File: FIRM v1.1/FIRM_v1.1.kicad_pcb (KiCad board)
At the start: 8 copper layers, 70 parts, among them J2 Conn_01x02_Pin, Q1 IRLML6402, U1 W25N04KVZEIR, U2 STM32H743VIHx, U3 ADXL371, U5 INA219AxDCN, U6 MIC5219-3.3YM5, U9 A-USBC-20F0-EA-GSR05, X1 32.768khz, Y1 12 MHz

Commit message: Added new flash chip
Set up quadSPI with the new 1gbit flash chip.
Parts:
- removed U1: W25N04KVZEIR, IC_W25N04KVZEIR:IC_W25N04KVZEIR

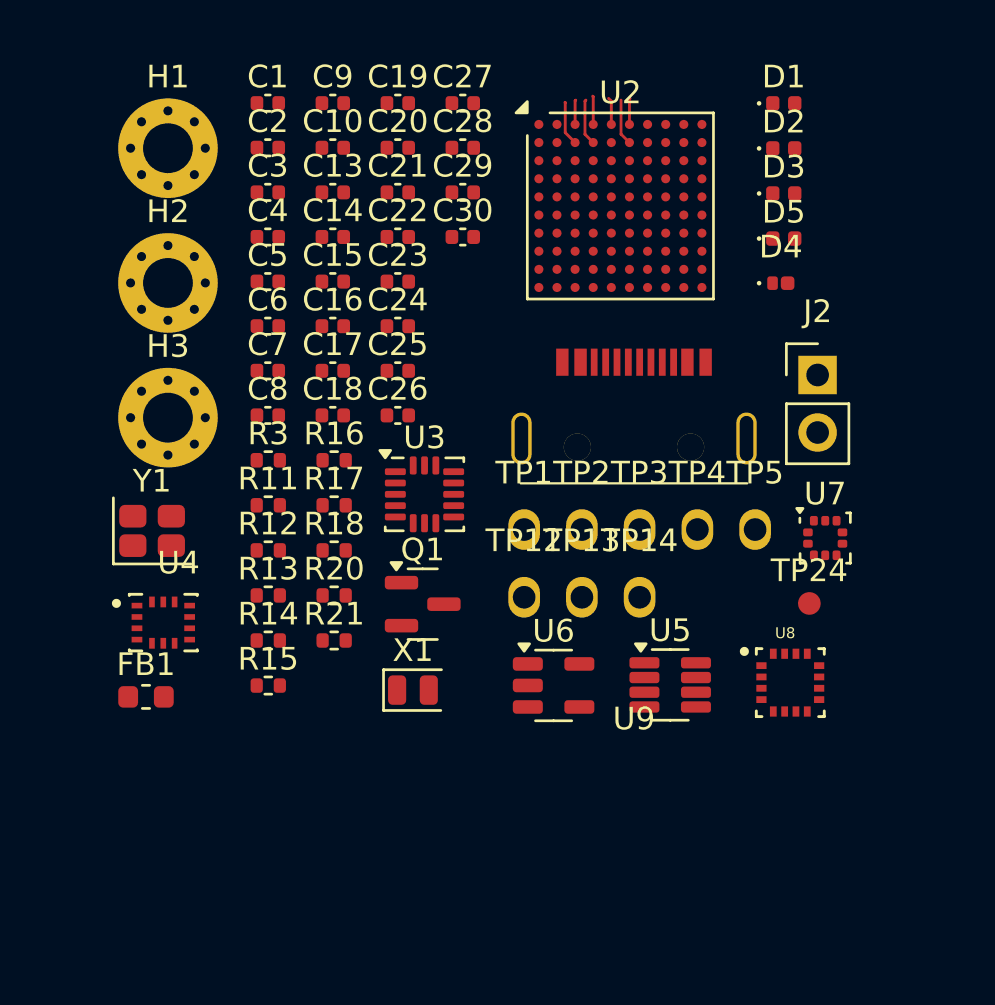
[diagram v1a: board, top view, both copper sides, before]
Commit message: added design rules
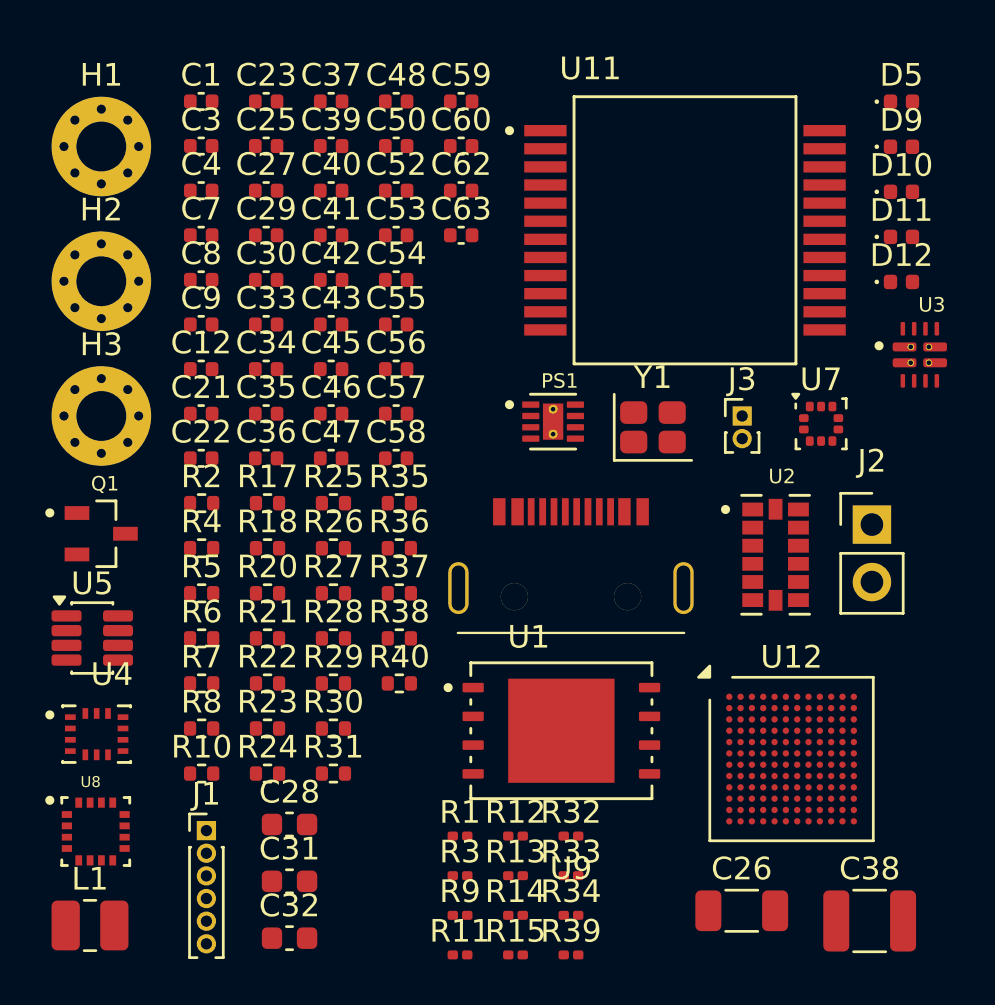
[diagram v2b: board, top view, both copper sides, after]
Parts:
- removed C10, C5: 14p, Capacitor_SMD:C_0402_1005Metric
- removed C13, C15, C17, C19, C20, C6: 100n, Capacitor_SMD:C_0402_1005Metric
- removed C14: 2u2, Capacitor_SMD:C_0402_1005Metric
- removed C16: 10n, Capacitor_SMD:C_0402_1005Metric
- removed C18: 1u, Capacitor_SMD:C_0402_1005Metric
- removed C2: 4u7, Capacitor_SMD:C_0402_1005Metric
- removed C24: 10u, Capacitor_SMD:C_0402_1005Metric
- removed D1: LED_Blue, LED_SMD:LED_0402_1005Metric
- removed D2: LED_Yellow, LED_SMD:LED_0402_1005Metric
- removed D3: LED_Red, LED_SMD:LED_0402_1005Metric
- removed D4: D_Schottky, connectors:D_schottky_NSR05F30NXT5G
- removed FB1: 120 Ohms @ 100 MHz, Inductor_SMD:L_0603_1608Metric
- removed R16: 100k, Resistor_SMD:R_0402_1005Metric
- removed TP1: PA0 Test Point, connectors:Testpoint_1.5x1.5mm_1.0mm
- removed TP12: SWDIO Through-Hole, connectors:Testpoint_1.5x1.5mm_1.0mm
- removed TP13: SWCLK Through-Hole, connectors:Testpoint_1.5x1.5mm_1.0mm
- removed TP14: 3.3V Test Point, connectors:Testpoint_1.5x1.5mm_1.0mm
- removed TP2: PA1 Test Point, connectors:Testpoint_1.5x1.5mm_1.0mm
- removed TP24: NRST Pad, connectors:smd_test_pads_1mm
- removed TP3: PA2 Test Point, connectors:Testpoint_1.5x1.5mm_1.0mm
- removed TP4: PA9 Test Point, connectors:Testpoint_1.5x1.5mm_1.0mm
- removed TP5: PA10 Test Point, connectors:Testpoint_1.5x1.5mm_1.0mm
- removed U6: MIC5219-3.3YM5, Package_TO_SOT_SMD:SOT-23-5
- removed X1: 32.768khz, connectors:Crystal_ECS-.327-6-12RR-TR
- added C12: 100n, Capacitor_SMD:C_0402_1005Metric, F.Cu at (140.8, 71.4)
- added C31: 22u, Capacitor_SMD:C_0603_1608Metric, F.Cu at (144.7, 94.0)
- added C32: 10u, Capacitor_SMD:C_0603_1608Metric, F.Cu at (144.7, 96.5)
- added C33: 1u, Capacitor_SMD:C_0402_1005Metric, F.Cu at (143.7, 69.4)
- added C34: 100n, Capacitor_SMD:C_0402_1005Metric, F.Cu at (143.7, 71.4)
- added C35: 100n, Capacitor_SMD:C_0402_1005Metric, F.Cu at (143.7, 73.4)
- added C36: 100n, Capacitor_SMD:C_0402_1005Metric, F.Cu at (143.7, 75.3)
- added C37: 1u, Capacitor_SMD:C_0402_1005Metric, F.Cu at (146.5, 59.6)
- added C38: 22u, Capacitor_SMD:C_1210_3225Metric, F.Cu at (170.3, 95.8)
- added C39: 100n, Capacitor_SMD:C_0402_1005Metric, F.Cu at (146.5, 61.6)
- added C40: 100n, Capacitor_SMD:C_0402_1005Metric, F.Cu at (146.5, 63.5)
- added C41: 100n, Capacitor_SMD:C_0402_1005Metric, F.Cu at (146.5, 65.5)
- added C42: 100n, Capacitor_SMD:C_0402_1005Metric, F.Cu at (146.5, 67.5)
- added C43: 100n, Capacitor_SMD:C_0402_1005Metric, F.Cu at (146.5, 69.4)
- added C45: 100n, Capacitor_SMD:C_0402_1005Metric, F.Cu at (146.5, 71.4)
- added C46: 14p, Capacitor_SMD:C_0402_1005Metric, F.Cu at (146.5, 73.4)
- added C47: 14p, Capacitor_SMD:C_0402_1005Metric, F.Cu at (146.5, 75.3)
- added C48: 100n, Capacitor_SMD:C_0402_1005Metric, F.Cu at (149.4, 59.6)
- added C50: 2u2, Capacitor_SMD:C_0402_1005Metric, F.Cu at (149.4, 61.6)
- added C52: 100n, Capacitor_SMD:C_0402_1005Metric, F.Cu at (149.4, 63.5)
- added C53: 2u2, Capacitor_SMD:C_0402_1005Metric, F.Cu at (149.4, 65.5)
- added C54: 100n, Capacitor_SMD:C_0402_1005Metric, F.Cu at (149.4, 67.5)
- added C55: 100n, Capacitor_SMD:C_0402_1005Metric, F.Cu at (149.4, 69.4)
- added C56: 1u, Capacitor_SMD:C_0402_1005Metric, F.Cu at (149.4, 71.4)
- added C57: 1u, Capacitor_SMD:C_0402_1005Metric, F.Cu at (149.4, 73.4)
- added C58: 100n, Capacitor_SMD:C_0402_1005Metric, F.Cu at (149.4, 75.3)
- added C59: 1u, Capacitor_SMD:C_0402_1005Metric, F.Cu at (152.3, 59.6)
- added C60: 1u, Capacitor_SMD:C_0402_1005Metric, F.Cu at (152.3, 61.6)
- added C62: 10u, Capacitor_SMD:C_0402_1005Metric, F.Cu at (152.3, 63.5)
- added C63: 1u, Capacitor_SMD:C_0402_1005Metric, F.Cu at (152.3, 65.5)
- added D10: LED_Yellow, LED_SMD:LED_0402_1005Metric, F.Cu at (171.7, 63.6)
- added D11: LED_Red, LED_SMD:LED_0402_1005Metric, F.Cu at (171.7, 65.6)
- added D12: LED_Green, LED_SMD:LED_0402_1005Metric, F.Cu at (171.7, 67.6)
- added D9: LED_Blue, LED_SMD:LED_0402_1005Metric, F.Cu at (171.7, 61.6)
- added J1: Pin, Connector_PinHeader_1.00mm:PinHeader_1x06_P1.00mm_Vertical, F.Cu at (141.0, 91.8)
- added J3: FIRM2 Conn, Connector_PinHeader_1.00mm:PinHeader_1x02_P1.00mm_Vertical, F.Cu at (164.7, 73.5)
- added L1: 2u2, Inductor_SMD:L_1008_2520Metric, F.Cu at (135.9, 96.0)
- added PS1: TPS62162DSGR, HPRC_Regulators:TPS62162DSGR, F.Cu at (156.3, 73.7)
- added R1: 0, Resistor_SMD:R_0201_0603Metric, F.Cu at (152.2, 92.0)
- added R10: 1k2, Resistor_SMD:R_0402_1005Metric, F.Cu at (140.8, 89.3)
- added R2: 10k, Resistor_SMD:R_0402_1005Metric, F.Cu at (140.8, 77.3)
- added R22: 10k, Resistor_SMD:R_0402_1005Metric, F.Cu at (143.7, 85.3)
- added R23: 10k, Resistor_SMD:R_0402_1005Metric, F.Cu at (143.7, 87.3)
- added R24: 10k, Resistor_SMD:R_0402_1005Metric, F.Cu at (143.7, 89.3)
- added R25: 10k, Resistor_SMD:R_0402_1005Metric, F.Cu at (146.6, 77.3)
- added R26: 100k, Resistor_SMD:R_0402_1005Metric, F.Cu at (146.6, 79.3)
- added R27: 100k, Resistor_SMD:R_0402_1005Metric, F.Cu at (146.6, 81.3)
- added R28: 80k, Resistor_SMD:R_0402_1005Metric, F.Cu at (146.6, 83.3)
- added R29: 100k, Resistor_SMD:R_0402_1005Metric, F.Cu at (146.6, 85.3)
- added R30: 7k6, Resistor_SMD:R_0402_1005Metric, F.Cu at (146.6, 87.3)
- added R31: 57.6k, Resistor_SMD:R_0402_1005Metric, F.Cu at (146.6, 89.3)
- added R32: 0, Resistor_SMD:R_0201_0603Metric, F.Cu at (157.1, 92.0)
- added R33: 0, Resistor_SMD:R_0201_0603Metric, F.Cu at (157.1, 93.8)
- added R34: 0, Resistor_SMD:R_0201_0603Metric, F.Cu at (157.1, 95.5)
- added R35: 5.1k, Resistor_SMD:R_0402_1005Metric, F.Cu at (149.5, 77.3)
- added R36: 10k, Resistor_SMD:R_0402_1005Metric, F.Cu at (149.5, 79.3)
- added R37: 32k, Resistor_SMD:R_0402_1005Metric, F.Cu at (149.5, 81.3)
- added R38: 100k, Resistor_SMD:R_0402_1005Metric, F.Cu at (149.5, 83.3)
- added R39: 0, Resistor_SMD:R_0201_0603Metric, F.Cu at (157.1, 97.3)
- added R4: 3k3, Resistor_SMD:R_0402_1005Metric, F.Cu at (140.8, 79.3)
- added R40: 1k, Resistor_SMD:R_0402_1005Metric, F.Cu at (149.5, 85.3)
- added R5: 3k3, Resistor_SMD:R_0402_1005Metric, F.Cu at (140.8, 81.3)
- added R6: 1.2k, Resistor_SMD:R_0402_1005Metric, F.Cu at (140.8, 83.3)
- added R7: 1k2, Resistor_SMD:R_0402_1005Metric, F.Cu at (140.8, 85.3)
- added R8: 1k2, Resistor_SMD:R_0402_1005Metric, F.Cu at (140.8, 87.3)
- added R9: 0, Resistor_SMD:R_0201_0603Metric, F.Cu at (152.2, 95.5)
- added U1: W25N01KVZEIR, HPRC_Storage:W25N01KVZEIR, F.Cu at (156.7, 87.4)
- added U11: SCH16T-K01-10, HPRC_Sensors:XDCR_SCH16T-K01-10, F.Cu at (162.2, 65.3)
- added U12: STM32F446ZCH6, Package_BGA:UFBGA-144_7x7mm_Layout12x12_P0.5mm, F.Cu at (166.9, 88.6)
- C26: value 470p -> 10u; footprint Capacitor_SMD:C_0402_1005Metric -> Capacitor_SMD:C_1206_3216Metric
- C28: footprint Capacitor_SMD:C_0402_1005Metric -> Capacitor_SMD:C_0603_1608Metric
- C4: value 6p -> 4u7
- C7: value 6p -> 100n
- C9: value 2u2 -> 100n
- J2: value Conn_01x02_Pin -> Vbat Jmpr; footprint connectors:power_headers -> HPRC_Connectors:power_headers
- Q1: value IRLML6402 -> DMP3098L-7; footprint Package_TO_SOT_SMD:SOT-23 -> HPRC_Logic:DMP3098L-7
- R11, R12: value 3k3 -> 0; footprint Resistor_SMD:R_0402_1005Metric -> Resistor_SMD:R_0201_0603Metric
- R13: value 1.2k -> 0; footprint Resistor_SMD:R_0402_1005Metric -> Resistor_SMD:R_0201_0603Metric
- R14, R15: value 1k2 -> 0; footprint Resistor_SMD:R_0402_1005Metric -> Resistor_SMD:R_0201_0603Metric
- R17: value 10m -> 100m
- R3: value 100k -> 0; footprint Resistor_SMD:R_0402_1005Metric -> Resistor_SMD:R_0201_0603Metric
- U2: value STM32H743VIHx -> ADXL375; footprint Package_BGA:TFBGA-100_8x8mm_Layout10x10_P0.8mm -> HPRC_Sensors:ADXL375BCCZ-RL7
- U3: value ADXL371 -> TPS2121RUXR; footprint Sensor_Motion:Analog_LGA-16_3.25x3mm_P0.5mm_LayoutBorder3x5y -> HPRC_Regulators:IC_TPS2121RUXR
- U4: value ~ -> ICM45686; footprint sensors:IC_ICM-45686 -> HPRC_Sensors:IC_ICM-45686
- U7: value ~ -> BMP581; footprint sensors:BMPFootprintNoSolderMask -> HPRC_Sensors:BMP581
- U8: value ~ -> MMC5983MA; footprint sensors:IC_MMC5983MA -> HPRC_Sensors:IC_MMC5983MA
- U9: footprint connectors:A-USBC-20F0-EA-GSR05 -> HPRC_Connectors:A-USBC-20F0-EA-GSR05
- Y1: footprint connectors:Crystal_ECS-120-10-36B2-CWY-TR -> HPRC_Connectors:Crystal_ECS-120-10-36B2-CWY-TR
- moved U8 31.4 mm to (136.1, 91.8)
- moved C28 30.8 mm to (144.7, 91.5)
- moved C26 26.6 mm to (164.7, 95.3)
- moved U5 25.6 mm to (136.0, 83.3)
- moved U3 22.7 mm to (172.5, 70.8)
- moved Y1 22.6 mm to (160.7, 74.0)
- moved R11 21.6 mm to (152.2, 97.3)
- moved R3 20.2 mm to (152.2, 93.8)
- moved U2 16.9 mm to (166.2, 79.6)
- moved R12 16.7 mm to (154.7, 92.0)
- moved R13 16.5 mm to (154.7, 93.8)
- moved R14 16.3 mm to (154.7, 95.5)
- moved R15 16.1 mm to (154.7, 97.3)
- moved Q1 14.5 mm to (136.4, 78.7)
- moved C22 13.1 mm to (140.8, 75.3)
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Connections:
- net VBAT renamed Net-(J2-Pin_1)
- C1 pad 1: unconnected-(C1-Pad1) -> +3.3V
- C26 pad 1: Net-(U6-BP) -> /VSENS_OUT
- C28 pad 1: +3.3V -> VBUS
- C4 pad 1: Net-(C4-Pad1) -> +3.3V
- C7 pad 1: Net-(C7-Pad1) -> +3.3V
- C9 pad 1: unconnected-(C9-Pad1) -> +3.3V
- Q1 pad 1: VBUS -> Net-(Q1-Pad1)
- Q1 pad 2: /VSENS_IN -> GND
- R11 pad 1: unconnected-(R11-Pad1) -> /QUADSPI_BK1_IO3
- R11 pad 2: +3.3V -> Net-(U12-PF6)
- R12 pad 1: unconnected-(R12-Pad1) -> Net-(U12-PF7)
- R12 pad 2: +3.3V -> /QUADSPI_BK1_IO2
- R13 pad 2: /DBUG_0 -> /QUADSPI_BK1_IO1
- R14 pad 2: /DBUG_1 -> /QUADSPI_BK1_IO0
- R15 pad 2: /DBUG_2 -> /SCK3
- R3 pad 1: unconnected-(R3-Pad1) -> /MISO2
- R3 pad 2: GND -> Net-(U12-PC2)
- U3 pad 1: +3.3V -> /VSENS_IN
- U3 pad 10: unconnected-(U3-GND-Pad13) -> Net-(U3-ILIM)
- U3 pad 11: /HIG_INT -> Net-(U3-SS)
- U3 pad 2: unconnected-(U3-NIC-Pad2) -> GND
- U3 pad 3: unconnected-(U3-RES-Pad3) -> Net-(U3-CP2)
- U3 pad 4: /SCK2 -> Net-(U3-OV2)
- U3 pad 5: unconnected-(U3-RES-Pad5) -> GND
- U3 pad 6: /MOSI2 -> Net-(U3-PR1)
- U3 pad 7: /MISO2 -> VBUS
- U3 pad 8: /HIG_CS -> /VSENS_IN
- U3 pad 9: unconnected-(U3-INT2-Pad9) -> GND
- Y1 pad 1: Net-(C5-Pad1) -> /RCC_OSC_IN
- Y1 pad 3: Net-(C10-Pad1) -> /RCC_OSC_OUT
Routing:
- net unconnected-(U2-PB8-PadB4): track 2.04 -> 0.00 mm
- net unconnected-(U2-PD5-PadB6): track 2.03 -> 0.00 mm
- net unconnected-(U2-PE3-PadB3): track 1.96 -> 0.00 mm
- net unconnected-(U2-PB9-PadA4): track 1.26 -> 0.00 mm
- net unconnected-(U2-PB7-PadA5): track 1.20 -> 0.00 mm
- net unconnected-(U2-PB4-PadA6): track 1.16 -> 0.00 mm
- net unconnected-(U2-PE2-PadA3): track 1.09 -> 0.00 mm

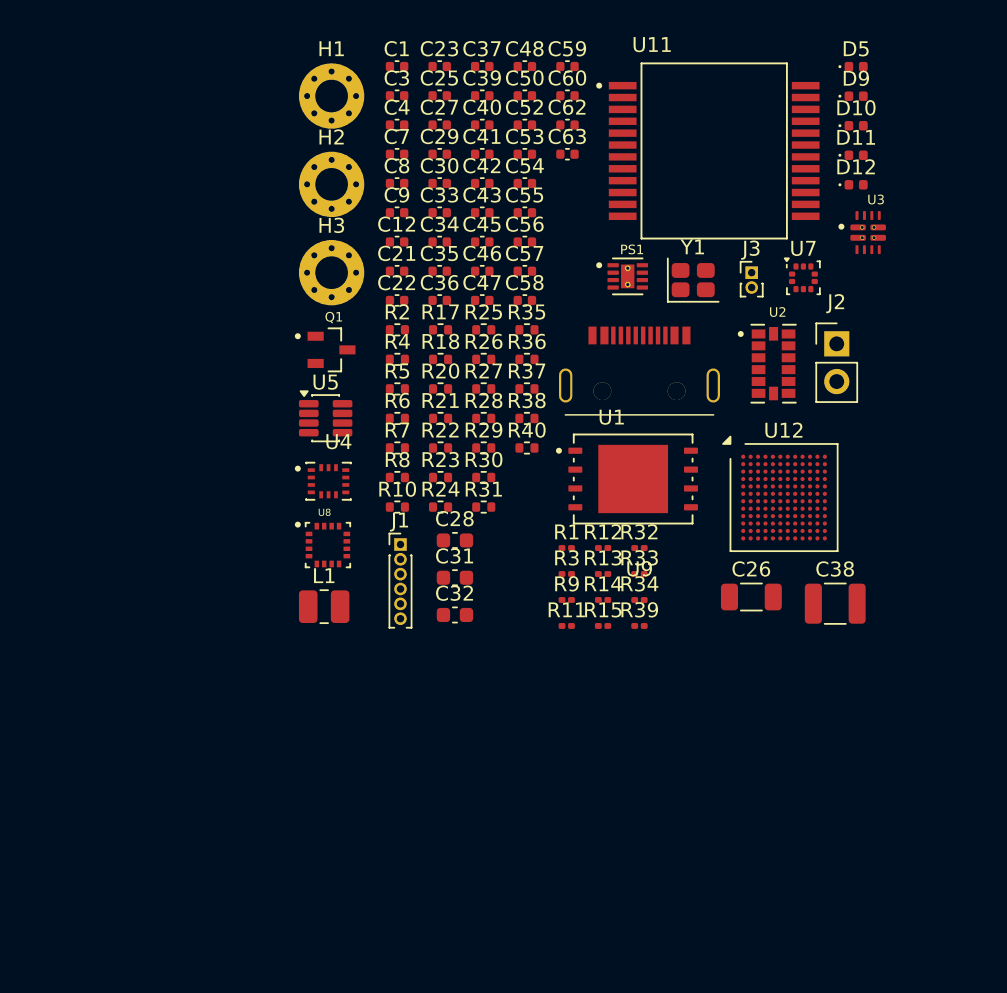
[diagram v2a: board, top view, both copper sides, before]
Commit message: Updated Footprints
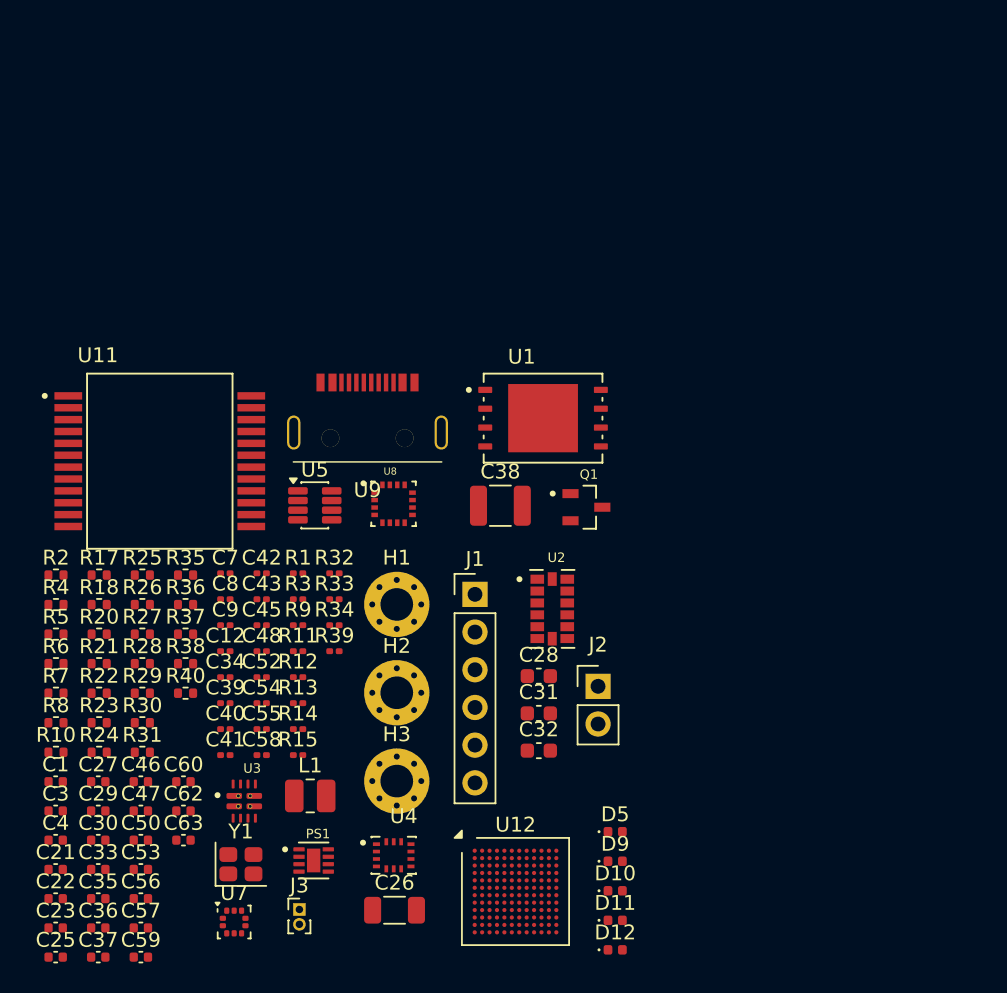
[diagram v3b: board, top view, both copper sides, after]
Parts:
- C12, C34, C39, C40, C41, C42, C43, C45, C48, C52, C54, C55, C58, C7, C8, C9: footprint Capacitor_SMD:C_0402_1005Metric -> Capacitor_SMD:C_0201_0603Metric
- J1: footprint Connector_PinHeader_1.00mm:PinHeader_1x06_P1.00mm_Vertical -> Connector_PinHeader_2.54mm:PinHeader_1x06_P2.54mm_Vertical
- moved C59 66.5 mm to (123.5, 119.6)
- moved C37 65.3 mm to (120.7, 119.6)
- moved C23 63.5 mm to (117.8, 117.6)
- moved C25 63.5 mm to (117.8, 119.6)
- moved U7 57.9 mm to (129.8, 117.2)
- moved U3 56.9 mm to (130.5, 109.1)
- moved C50 56.4 mm to (123.5, 111.7)
- moved C53 54.7 mm to (123.5, 113.7)
- moved D11 54.0 mm to (155.5, 117.1)
- moved D5 54.0 mm to (155.5, 111.1)
- moved D9 54.0 mm to (155.5, 113.1)
- moved D10 54.0 mm to (155.5, 115.1)
- moved D12 54.0 mm to (155.5, 119.1)
- moved C1 53.4 mm to (117.8, 107.8)
- moved C3 53.4 mm to (117.8, 109.7)
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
